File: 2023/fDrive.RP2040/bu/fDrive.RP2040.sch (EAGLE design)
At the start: 11 parts

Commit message: update
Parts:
- removed WRITE_DISABLED: (no value), microbuilder:SOLDERJUMPER
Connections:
- removed net MCU_VCC_5V: MCU_LEFT_SIDE.7
- removed net WP: FLASH_AT25SF321B_4MB.!WP, WRITE_DISABLED.2
- net GND: no longer WRITE_DISABLED.1
- net VCC_33: now also FLASH_AT25SF321B_4MB.!WP
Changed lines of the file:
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@@
 <part name="RUNNING" library="adafruit" deviceset="LED" device="SMT1206"/>
 <part name="MODE" library="switch-omron" library_urn="urn:adsk.eagle:library:377" deviceset="10-XX" device="" package3d_urn="urn:adsk.eagle:package:27496/1"/>
-<part name="WRITE_DISABLED" library="microbuilder" deviceset="SOLDERJUMPER" device=""/>
 <part name="FLASH_AT25SF321B_4MB" library="microchip" library_urn="urn:adsk.eagle:library:294" deviceset="25*" device="SN" package3d_urn="urn:adsk.eagle:package:20804/2" technology="AA080"/>
 <part name="GND3" library="supply1" deviceset="GND" device=""/>
-<part name="GND4" library="supply1" deviceset="GND" device=""/>
 <part name="AUTHORIZE" library="switch-omron" library_urn="urn:adsk.eagle:library:377" deviceset="10-XX" device="" package3d_urn="urn:adsk.eagle:package:27496/1"/>
 <part name="BUTTON_PRESSED" library="adafruit" deviceset="LED" device="SMT1206"/>
@@
 <attribute name="VALUE" x="-120.65" y="109.855" size="1.778" layer="96" rot="R90"/>
 </instance>
-<instance part="WRITE_DISABLED" gate="1" x="-45.72" y="165.1" smashed="yes">
-<attribute name="NAME" x="-55.88" y="160.02" size="1.778" layer="95"/>
-<attribute name="VALUE" x="-48.26" y="161.29" size="1.778" layer="96"/>
-</instance>
 <instance part="FLASH_AT25SF321B_4MB" gate="G$1" x="2.54" y="154.94" smashed="yes">
 <attribute name="NAME" x="-7.62" y="166.27" size="1.778" layer="95"/>
@@
 <instance part="GND3" gate="1" x="10.16" y="137.16" smashed="yes">
 <attribute name="VALUE" x="7.62" y="134.62" size="1.778" layer="96" rot="R180"/>
-</instance>
-<instance part="GND4" gate="1" x="-73.66" y="165.1" smashed="yes" rot="R270">
-<attribute name="VALUE" x="-76.2" y="167.64" size="1.778" layer="96" rot="R90"/>
 </instance>
 <instance part="AUTHORIZE" gate="1" x="-127" y="154.94" smashed="yes">
@@
 <wire x1="10.16" y1="139.7" x2="10.16" y2="144.78" width="0.1524" layer="91"/>
 </segment>
-<segment>
-<pinref part="GND4" gate="1" pin="GND"/>
-<pinref part="WRITE_DISABLED" gate="1" pin="1"/>
-<wire x1="-71.12" y1="165.1" x2="-50.8" y2="165.1" width="0.1524" layer="91"/>
-</segment>
 </net>
 <net name="VCC_33" class="0">
@@
 <label x="-27.94" y="147.32" size="1.778" layer="95"/>
 </segment>
+<segment>
+<pinref part="FLASH_AT25SF321B_4MB" gate="G$1" pin="!WP"/>
+<wire x1="-10.16" y1="162.56" x2="-20.32" y2="162.56" width="0.1524" layer="91"/>
+<label x="-17.78" y="165.1" size="1.778" layer="95"/>
+</segment>
 </net>
 <net name="MCU_D6" class="0">
@@
 </segment>
 </net>
-<net name="MCU_VCC_5V" class="0">
-<segment>
-<pinref part="MCU_LEFT_SIDE" gate="A" pin="7"/>
-<wire x1="7.62" y1="124.46" x2="7.62" y2="111.76" width="0.1524" layer="91"/>
-<label x="7.62" y="111.76" size="1.778" layer="95" rot="R270"/>
-</segment>
-</net>
 <net name="RA_1" class="0">
 <segment>
@@
 </segment>
 </net>
-<net name="WP" class="0">
-<segment>
-<pinref part="FLASH_AT25SF321B_4MB" gate="G$1" pin="!WP"/>
-<wire x1="-10.16" y1="162.56" x2="-20.32" y2="162.56" width="0.1524" layer="91"/>
-<label x="-17.78" y="165.1" size="1.778" layer="95"/>
-</segment>
-<segment>
-<pinref part="WRITE_DISABLED" gate="1" pin="2"/>
-<wire x1="-40.64" y1="165.1" x2="-27.94" y2="165.1" width="0.1524" layer="91"/>
-<label x="-35.56" y="167.64" size="1.778" layer="95"/>
-</segment>
-</net>

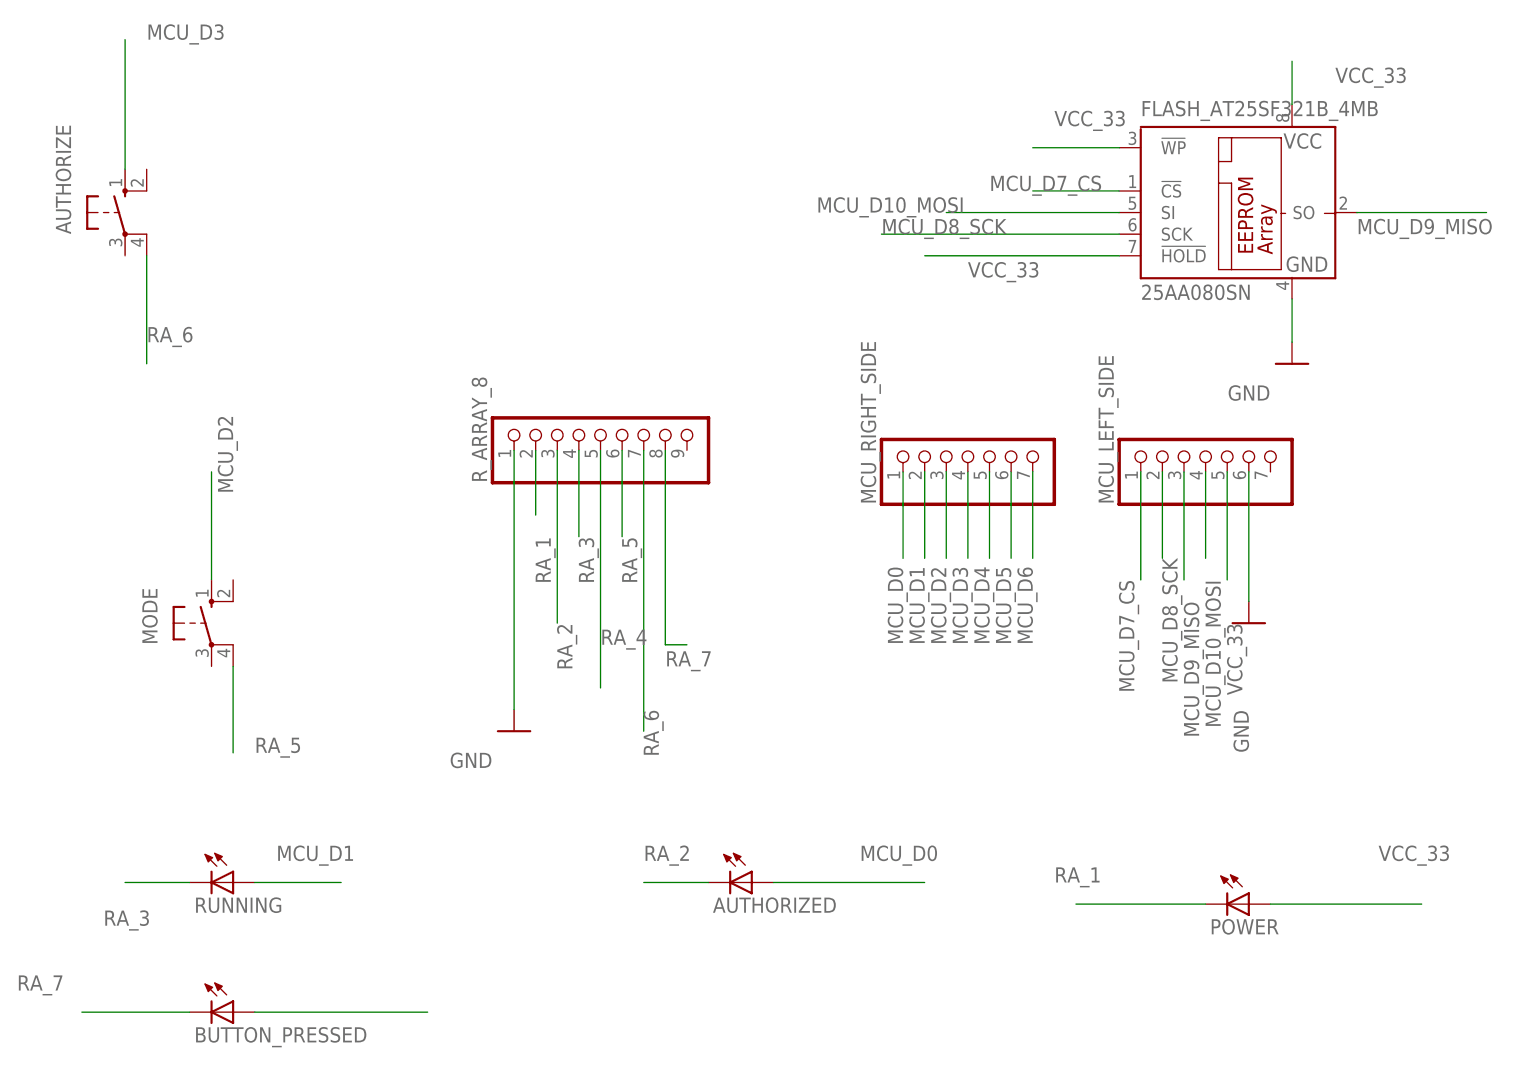
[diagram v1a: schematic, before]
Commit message: Nusbio I2C Extension
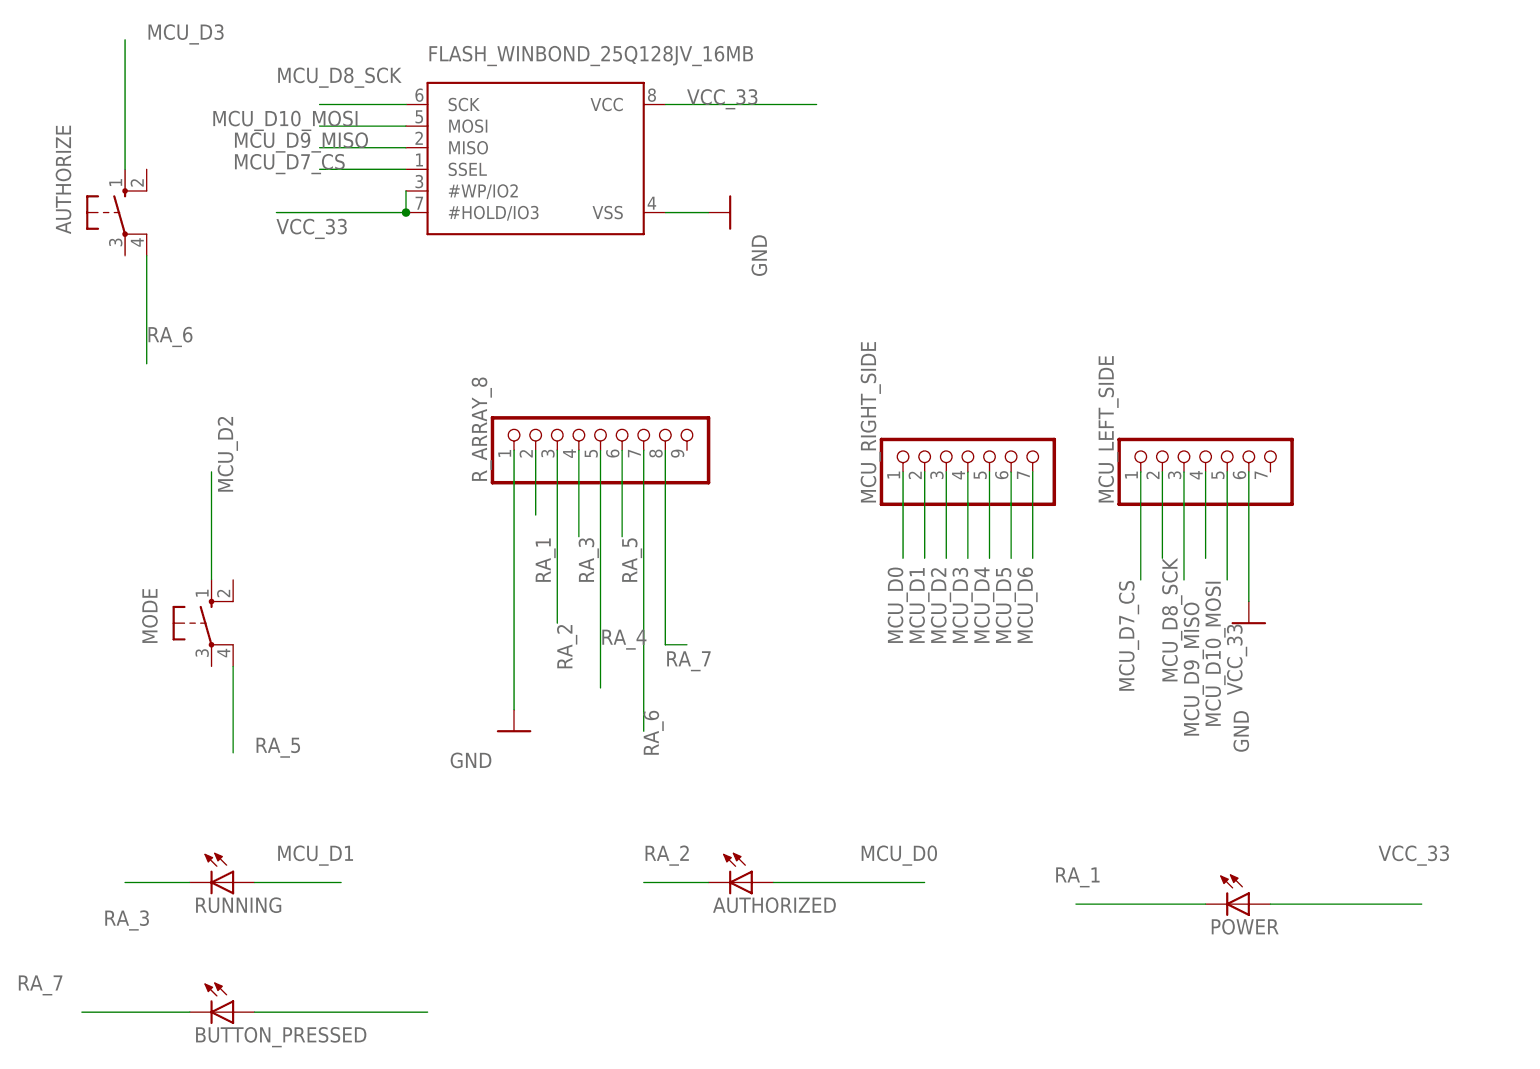
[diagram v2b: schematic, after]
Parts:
- removed FLASH_AT25SF321B_4MB: 25AA080SN, microchip:25AA080SN
- added FLASH_WINBOND_25Q128JV_16MB: (no value), microbuilder:SPIFLASH_SOIC8208MIL
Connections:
- net GND: now also FLASH_WINBOND_25Q128JV_16MB.VSS; no longer FLASH_AT25SF321B_4MB.GND
- net MCU_D10_MOSI: now also FLASH_WINBOND_25Q128JV_16MB.MOSI; no longer FLASH_AT25SF321B_4MB.SI
- net MCU_D7_CS: now also FLASH_WINBOND_25Q128JV_16MB.SSEL; no longer FLASH_AT25SF321B_4MB.!CS
- net MCU_D8_SCK: now also FLASH_WINBOND_25Q128JV_16MB.SCK; no longer FLASH_AT25SF321B_4MB.SCK
- net MCU_D9_MISO: now also FLASH_WINBOND_25Q128JV_16MB.MISO; no longer FLASH_AT25SF321B_4MB.SO
- net VCC_33: now also FLASH_WINBOND_25Q128JV_16MB.#HOLD/IO3, FLASH_WINBOND_25Q128JV_16MB.#WP/IO2, FLASH_WINBOND_25Q128JV_16MB.VCC; no longer FLASH_AT25SF321B_4MB.!HOLD, FLASH_AT25SF321B_4MB.!WP, FLASH_AT25SF321B_4MB.VCC
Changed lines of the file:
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@@
 <part name="RUNNING" library="adafruit" deviceset="LED" device="SMT1206"/>
 <part name="MODE" library="switch-omron" library_urn="urn:adsk.eagle:library:377" deviceset="10-XX" device="" package3d_urn="urn:adsk.eagle:package:27496/1"/>
-<part name="FLASH_AT25SF321B_4MB" library="microchip" library_urn="urn:adsk.eagle:library:294" deviceset="25*" device="SN" package3d_urn="urn:adsk.eagle:package:20804/2" technology="AA080"/>
-<part name="GND3" library="supply1" deviceset="GND" device=""/>
 <part name="AUTHORIZE" library="switch-omron" library_urn="urn:adsk.eagle:library:377" deviceset="10-XX" device="" package3d_urn="urn:adsk.eagle:package:27496/1"/>
 <part name="BUTTON_PRESSED" library="adafruit" deviceset="LED" device="SMT1206"/>
+<part name="FLASH_WINBOND_25Q128JV_16MB" library="microbuilder" deviceset="SPIFLASH_SOIC8" device="208MIL"/>
+<part name="GND4" library="supply1" deviceset="GND" device=""/>
 </parts>
 <sheets>
@@
 <attribute name="VALUE" x="-120.65" y="109.855" size="1.778" layer="96" rot="R90"/>
 </instance>
-<instance part="FLASH_AT25SF321B_4MB" gate="G$1" x="2.54" y="154.94" smashed="yes">
-<attribute name="NAME" x="-7.62" y="166.27" size="1.778" layer="95"/>
-<attribute name="VALUE" x="-7.62" y="144.68" size="1.778" layer="96"/>
-</instance>
-<instance part="GND3" gate="1" x="10.16" y="137.16" smashed="yes">
-<attribute name="VALUE" x="7.62" y="134.62" size="1.778" layer="96" rot="R180"/>
-</instance>
 <instance part="AUTHORIZE" gate="1" x="-127" y="154.94" smashed="yes">
 <attribute name="NAME" x="-133.35" y="152.4" size="1.778" layer="95" rot="R90"/>
@@
 <attribute name="NAME" x="-118.872" y="57.404" size="1.778" layer="95"/>
 <attribute name="VALUE" x="-118.872" y="55.245" size="1.778" layer="96"/>
+</instance>
+<instance part="FLASH_WINBOND_25Q128JV_16MB" gate="G$1" x="-78.74" y="160.02" smashed="yes">
+<attribute name="NAME" x="-91.44" y="172.72" size="1.778" layer="95"/>
+<attribute name="VALUE" x="-91.44" y="149.86" size="1.778" layer="95"/>
+</instance>
+<instance part="GND4" gate="1" x="-55.88" y="154.94" smashed="yes" rot="R90">
+<attribute name="VALUE" x="-53.34" y="152.4" size="1.778" layer="96" rot="R270"/>
 </instance>
 </instances>
@@
 </segment>
 <segment>
-<pinref part="GND3" gate="1" pin="GND"/>
-<pinref part="FLASH_AT25SF321B_4MB" gate="G$1" pin="GND"/>
-<wire x1="10.16" y1="139.7" x2="10.16" y2="144.78" width="0.1524" layer="91"/>
+<pinref part="FLASH_WINBOND_25Q128JV_16MB" gate="G$1" pin="VSS"/>
+<pinref part="GND4" gate="1" pin="GND"/>
+<wire x1="-63.5" y1="154.94" x2="-58.42" y2="154.94" width="0.1524" layer="91"/>
 </segment>
 </net>
@@
 </segment>
 <segment>
-<pinref part="FLASH_AT25SF321B_4MB" gate="G$1" pin="VCC"/>
-<wire x1="10.16" y1="167.64" x2="10.16" y2="172.72" width="0.1524" layer="91"/>
-<label x="15.24" y="170.18" size="1.778" layer="95"/>
-</segment>
-<segment>
-<pinref part="FLASH_AT25SF321B_4MB" gate="G$1" pin="!HOLD"/>
-<wire x1="-10.16" y1="149.86" x2="-33.02" y2="149.86" width="0.1524" layer="91"/>
-<label x="-27.94" y="147.32" size="1.778" layer="95"/>
-</segment>
-<segment>
-<pinref part="FLASH_AT25SF321B_4MB" gate="G$1" pin="!WP"/>
-<wire x1="-10.16" y1="162.56" x2="-20.32" y2="162.56" width="0.1524" layer="91"/>
-<label x="-17.78" y="165.1" size="1.778" layer="95"/>
+<pinref part="FLASH_WINBOND_25Q128JV_16MB" gate="G$1" pin="VCC"/>
+<wire x1="-63.5" y1="167.64" x2="-45.72" y2="167.64" width="0.1524" layer="91"/>
+<label x="-60.96" y="167.64" size="1.778" layer="95"/>
+</segment>
+<segment>
+<pinref part="FLASH_WINBOND_25Q128JV_16MB" gate="G$1" pin="#HOLD/IO3"/>
+<wire x1="-93.98" y1="154.94" x2="-109.22" y2="154.94" width="0.1524" layer="91"/>
+<pinref part="FLASH_WINBOND_25Q128JV_16MB" gate="G$1" pin="#WP/IO2"/>
+<wire x1="-93.98" y1="157.48" x2="-93.98" y2="154.94" width="0.1524" layer="91"/>
+<junction x="-93.98" y="154.94"/>
+<label x="-109.22" y="152.4" size="1.778" layer="95"/>
 </segment>
 </net>
@@
 </segment>
 <segment>
-<pinref part="FLASH_AT25SF321B_4MB" gate="G$1" pin="!CS"/>
-<wire x1="-10.16" y1="157.48" x2="-20.32" y2="157.48" width="0.1524" layer="91"/>
-<label x="-25.4" y="157.48" size="1.778" layer="95"/>
+<pinref part="FLASH_WINBOND_25Q128JV_16MB" gate="G$1" pin="SSEL"/>
+<wire x1="-93.98" y1="160.02" x2="-104.14" y2="160.02" width="0.1524" layer="91"/>
+<label x="-114.3" y="160.02" size="1.778" layer="95"/>
 </segment>
 </net>
@@
 </segment>
 <segment>
-<pinref part="FLASH_AT25SF321B_4MB" gate="G$1" pin="SCK"/>
-<wire x1="-10.16" y1="152.4" x2="-38.1" y2="152.4" width="0.1524" layer="91"/>
-<label x="-38.1" y="152.4" size="1.778" layer="95"/>
+<pinref part="FLASH_WINBOND_25Q128JV_16MB" gate="G$1" pin="SCK"/>
+<wire x1="-93.98" y1="167.64" x2="-104.14" y2="167.64" width="0.1524" layer="91"/>
+<label x="-109.22" y="170.18" size="1.778" layer="95"/>
 </segment>
 </net>
@@
 </segment>
 <segment>
-<pinref part="FLASH_AT25SF321B_4MB" gate="G$1" pin="SO"/>
-<wire x1="17.78" y1="154.94" x2="33.02" y2="154.94" width="0.1524" layer="91"/>
-<label x="17.78" y="152.4" size="1.778" layer="95"/>
+<pinref part="FLASH_WINBOND_25Q128JV_16MB" gate="G$1" pin="MISO"/>
+<wire x1="-93.98" y1="162.56" x2="-104.14" y2="162.56" width="0.1524" layer="91"/>
+<label x="-114.3" y="162.56" size="1.778" layer="95"/>
 </segment>
 </net>
@@
 </segment>
 <segment>
-<pinref part="FLASH_AT25SF321B_4MB" gate="G$1" pin="SI"/>
-<wire x1="-10.16" y1="154.94" x2="-30.48" y2="154.94" width="0.1524" layer="91"/>
-<label x="-45.72" y="154.94" size="1.778" layer="95"/>
-</segment>
-</net>
+<pinref part="FLASH_WINBOND_25Q128JV_16MB" gate="G$1" pin="MOSI"/>
+<wire x1="-93.98" y1="165.1" x2="-104.14" y2="165.1" width="0.1524" layer="91"/>
+<label x="-116.84" y="165.1" size="1.778" layer="95"/>
+</segment>
+</net>
